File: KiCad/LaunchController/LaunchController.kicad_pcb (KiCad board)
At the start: 2 copper layers, 150 x 100 mm, 164 parts, among them J1 CONN_ICSP, J10 CONN_AUDIO, J11 RJ45, J12 CONN_SPEAKER, J2 CONN_USB, J3 USB_B_Micro, J4 DC_IN, J5 TO_CONVERTER, J6 FROM_CONVERTER, J7 CONN_STATUS_PANEL, J8 CONN_PANEL_BAORD_2, J9 CONN_PANEL_BAORD_1, Q1 TJ8S06M3L, Q2 TJ8S06M3L, Q3 2SC3325-Y, SW1 SW_Push, SW11 SW_Push, SW12 SW_Push, SW13 SW_Push, SW14 SW_Push, SW15 SW_Push, SW16 SW_Push, SW17 SW_Push, SW18 SW_Push, SW19 SW_Push, SW2 SW_Push, SW20 SW_Push, SW21 SW_Push, SW22 SW_Push, SW23 SW_Push, SW24 SW_Push, SW25 SW_Push, U1 FT232RL, U2 ATMEGA2560-16AUR, U3 NJM7805SDL1, U4 INA219BIDCNT, U5 INA219BIDCNT, U6 DFPlayer, U7 24LC256, U8 LTC485CN8#PBF, Y1 HUSG-16.000-20

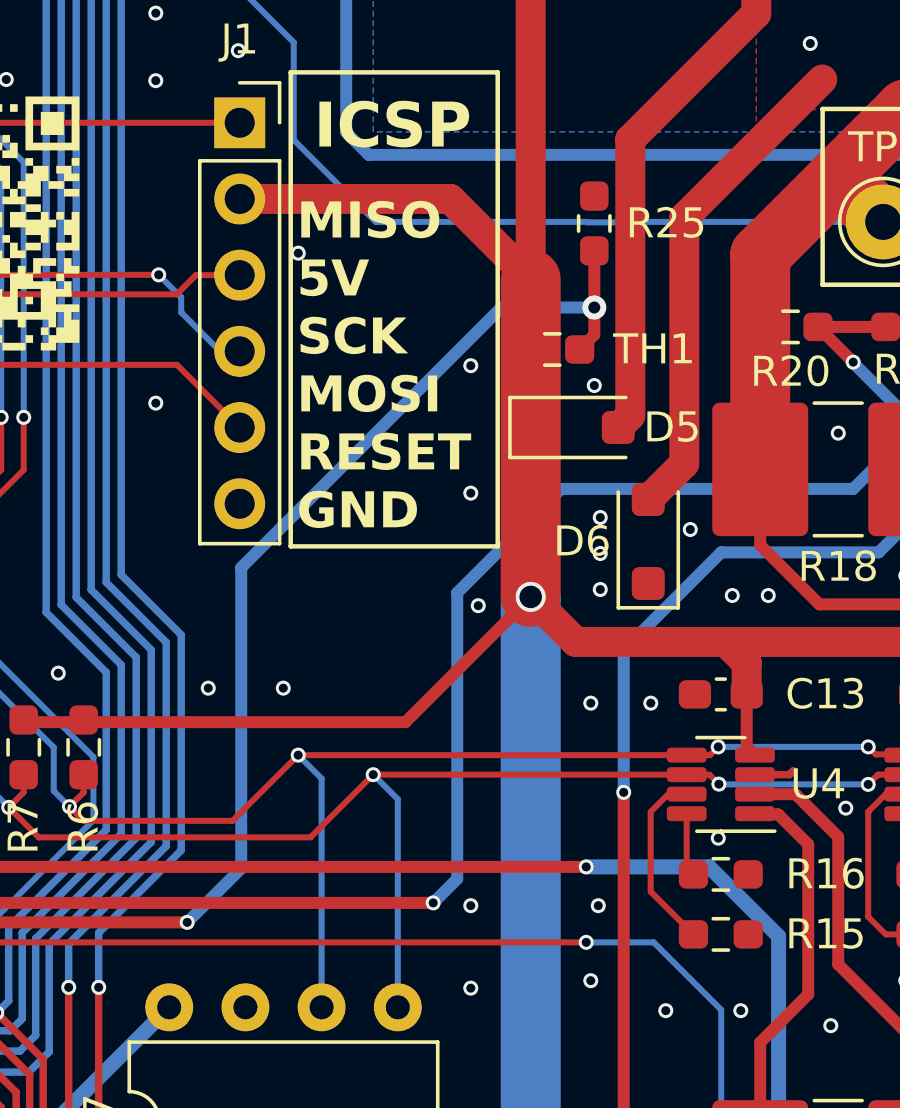
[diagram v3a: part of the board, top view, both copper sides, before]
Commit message: サーミスタを分圧の下流側に変更
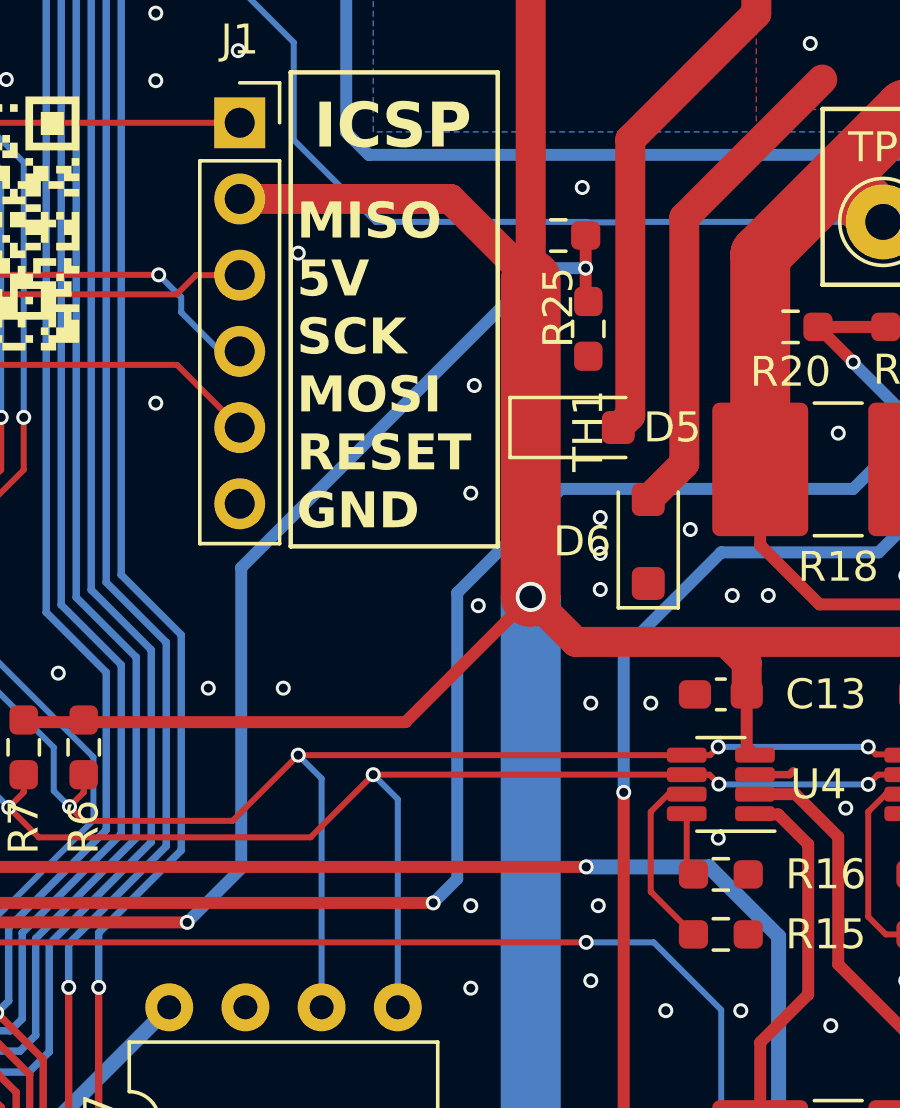
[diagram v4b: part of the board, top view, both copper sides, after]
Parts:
- moved TH1 1.38 mm to (157.8, 66.9), turned to -90 degrees
- moved R25 1.26 mm to (156.8, 63.8), turned to 180 degrees
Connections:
- R25 pad 1: GND -> VREF_THERMISTOR
- R25 pad 2: VREF_THERMISTOR -> CONN_LED_5V
- TH1 pad 1: CONN_LED_5V -> VREF_THERMISTOR
- TH1 pad 2: VREF_THERMISTOR -> GND
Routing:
- net VREF_THERMISTOR: track 46.9 -> 45.9 mm
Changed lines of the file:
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@@
   )
   (footprint "Resistor_SMD:R_0603_1608Metric_Pad0.98x0.95mm_HandSolder" (layer "F.Cu")
-    (at 156.6 67.6)
+    (at 157.8 66.9125 -90)
     (descr "Resistor SMD 0603 (1608 Metric), square (rectangular) end terminal, IPC_7351 nominal with elongated pad for handsoldering. (Body size source: IPC-SM-782 page 72, https://www.pcb-3d.com/wordpress/wp-content/uploads/ipc-sm-782a_amendment_1_and_2.pdf), generated with kicad-footprint-generator")
     (tags "resistor handsolder")
@@
     (property "ki_keywords" "thermistor NTC resistor sensor RTD")
     (attr smd)
-    (fp_text reference "TH1" (at 3.4 0 180) (layer "F.SilkS")
+    (fp_text reference "TH1" (at 3.4 0 90) (layer "F.SilkS")
         (effects (font (size 1 1) (thickness 0.15)))
     )
-    (fp_text value "10kR" (at 0 1.43) (layer "F.Fab")
+    (fp_text value "10kR" (at 0 1.43 90) (layer "F.Fab")
         (effects (font (size 1 1) (thickness 0.15)))
     )
-    (fp_text user "${REFERENCE}" (at 0 0) (layer "F.Fab")
+    (fp_text user "${REFERENCE}" (at 0 0 90) (layer "F.Fab")
         (effects (font (size 0.4 0.4) (thickness 0.06)))
     )
@@
     (fp_line (start 0.8 0.4125) (end -0.8 0.4125)
       (stroke (width 0.1) (type solid)) (layer "F.Fab"))
-    (pad "1" smd roundrect (at -0.9125 0) (size 0.975 0.95) (layers "F.Cu" "F.Paste" "F.Mask") (roundrect_rratio 0.25)
-      (net 40 "CONN_LED_5V") (pintype "passive"))
-    (pad "2" smd roundrect (at 0.9125 0) (size 0.975 0.95) (layers "F.Cu" "F.Paste" "F.Mask") (roundrect_rratio 0.25)
+    (pad "1" smd roundrect (at -0.9125 0 270) (size 0.975 0.95) (layers "F.Cu" "F.Paste" "F.Mask") (roundrect_rratio 0.25)
       (net 71 "VREF_THERMISTOR") (pintype "passive"))
+    (pad "2" smd roundrect (at 0.9125 0 270) (size 0.975 0.95) (layers "F.Cu" "F.Paste" "F.Mask") (roundrect_rratio 0.25)
+      (net 1 "GND") (pintype "passive"))
     (model "${KICAD6_3DMODEL_DIR}/Resistor_SMD.3dshapes/R_0603_1608Metric.wrl"
       (offset (xyz 0 0 0))
@@
   )
   (footprint "Resistor_SMD:R_0603_1608Metric_Pad0.98x0.95mm_HandSolder" (layer "F.Cu")
-    (at 158 63.4 -90)
+    (at 156.8 63.8 180)
     (descr "Resistor SMD 0603 (1608 Metric), square (rectangular) end terminal, IPC_7351 nominal with elongated pad for handsoldering. (Body size source: IPC-SM-782 page 72, https://www.pcb-3d.com/wordpress/wp-content/uploads/ipc-sm-782a_amendment_1_and_2.pdf), generated with kicad-footprint-generator")
     (tags "resistor handsolder")
@@
     (property "ki_keywords" "R resistor")
     (attr smd)
-    (fp_text reference "R25" (at 0 -2.4) (layer "F.SilkS")
+    (fp_text reference "R25" (at 0 -2.4 90) (layer "F.SilkS")
         (effects (font (size 1 1) (thickness 0.15)))
     )
-    (fp_text value "10kR" (at 0 1.43 90) (layer "F.Fab")
+    (fp_text value "10kR" (at 0 1.43) (layer "F.Fab")
         (effects (font (size 1 1) (thickness 0.15)))
     )
-    (fp_text user "${REFERENCE}" (at 0 0 90) (layer "F.Fab")
+    (fp_text user "${REFERENCE}" (at 0 0) (layer "F.Fab")
         (effects (font (size 0.4 0.4) (thickness 0.06)))
     )
@@
     (fp_line (start 0.8 0.4125) (end -0.8 0.4125)
       (stroke (width 0.1) (type solid)) (layer "F.Fab"))
-    (pad "1" smd roundrect (at -0.9125 0 270) (size 0.975 0.95) (layers "F.Cu" "F.Paste" "F.Mask") (roundrect_rratio 0.25)
-      (net 1 "GND") (pintype "passive"))
-    (pad "2" smd roundrect (at 0.9125 0 270) (size 0.975 0.95) (layers "F.Cu" "F.Paste" "F.Mask") (roundrect_rratio 0.25)
+    (pad "1" smd roundrect (at -0.9125 0 180) (size 0.975 0.95) (layers "F.Cu" "F.Paste" "F.Mask") (roundrect_rratio 0.25)
       (net 71 "VREF_THERMISTOR") (pintype "passive"))
+    (pad "2" smd roundrect (at 0.9125 0 180) (size 0.975 0.95) (layers "F.Cu" "F.Paste" "F.Mask") (roundrect_rratio 0.25)
+      (net 40 "CONN_LED_5V") (pintype "passive"))
     (model "${KICAD6_3DMODEL_DIR}/Resistor_SMD.3dshapes/R_0603_1608Metric.wrl"
       (offset (xyz 0 0 0))
@@
   (via (at 77.8 71.2) (size 0.5) (drill 0.3) (layers "F.Cu" "B.Cu") (free) (net 1))
   (via (at 127.883174 91.638716) (size 0.5) (drill 0.3) (layers "F.Cu" "B.Cu") (free) (net 1))
-  (via (at 153.883174 68.138716) (size 0.5) (drill 0.3) (layers "F.Cu" "B.Cu") (free) (net 1))
+  (via (at 154 68.8) (size 0.5) (drill 0.3) (layers "F.Cu" "B.Cu") (free) (net 1))
   (via (at 162.883174 89.638716) (size 0.5) (drill 0.3) (layers "F.Cu" "B.Cu") (free) (net 1))
   (via (at 91.4 86) (size 0.5) (drill 0.3) (layers "F.Cu" "B.Cu") (free) (net 1))
@@
   (via (at 88.6 40) (size 0.5) (drill 0.3) (layers "F.Cu" "B.Cu") (free) (net 1))
   (via (at 156.633174 122.388716) (size 0.5) (drill 0.3) (layers "F.Cu" "B.Cu") (free) (net 1))
-  (via (at 158 68.8) (size 0.5) (drill 0.3) (layers "F.Cu" "B.Cu") (free) (net 1))
   (via (at 172.4 112.8) (size 0.5) (drill 0.3) (layers "F.Cu" "B.Cu") (free) (net 1))
   (via (at 107 110) (size 0.5) (drill 0.3) (layers "F.Cu" "B.Cu") (free) (net 1))
   (via (at 191.383174 99.138716) (size 0.5) (drill 0.3) (layers "F.Cu" "B.Cu") (free) (net 1))
   (via (at 181.633174 99.388716) (size 0.5) (drill 0.3) (layers "F.Cu" "B.Cu") (free) (net 1))
+  (via (at 157.6 62.2) (size 0.5) (drill 0.3) (layers "F.Cu" "B.Cu") (free) (net 1))
   (via (at 84.8 83.8) (size 0.5) (drill 0.3) (layers "F.Cu" "B.Cu") (free) (net 1))
   (via (at 70.8 88.4) (size 0.5) (drill 0.3) (layers "F.Cu" "B.Cu") (free) (net 1))
@@
   (segment (start 131.955974 86.636526) (end 129.81668 84.497232) (width 0.25) (layer "F.Cu") (net 71))
   (segment (start 132.015741 86.696293) (end 144.430707 86.696293) (width 0.4) (layer "F.Cu") (net 71))
+  (segment (start 157.7125 64.8875) (end 157.7125 65.9125) (width 0.4) (layer "F.Cu") (net 71))
+  (segment (start 157.7125 65.9125) (end 157.8 66) (width 0.4) (layer "F.Cu") (net 71))
+  (segment (start 157.7125 64.8875) (end 157.7125 63.8) (width 0.4) (layer "F.Cu") (net 71))
   (segment (start 131.955974 86.636526) (end 132.015741 86.696293) (width 0.4) (layer "F.Cu") (net 71))
-  (segment (start 158 67.1125) (end 158 64.3125) (width 0.4) (layer "F.Cu") (net 71))
-  (segment (start 157.5125 67.6) (end 158 67.1125) (width 0.4) (layer "F.Cu") (net 71))
-  (via (at 158 66.2) (size 0.8) (drill 0.4) (layers "F.Cu" "B.Cu") (net 71))
+  (via (at 157.7125 64.8875) (size 0.5) (drill 0.3) (layers "F.Cu" "B.Cu") (net 71))
   (via (at 144.430707 86.696293) (size 0.5) (drill 0.3) (layers "F.Cu" "B.Cu") (net 71))
-  (segment (start 144.430707 86.696293) (end 146.230707 84.896293) (width 0.4) (layer "B.Cu") (net 71))
   (segment (start 146.230707 74.871944) (end 146.230707 84.896293) (width 0.4) (layer "B.Cu") (net 71))
-  (segment (start 154.902651 66.2) (end 146.230707 74.871944) (width 0.4) (layer "B.Cu") (net 71))
-  (segment (start 158 66.2) (end 154.902651 66.2) (width 0.4) (layer "B.Cu") (net 71))
+  (segment (start 146.230707 84.896293) (end 144.430707 86.696293) (width 0.4) (layer "B.Cu") (net 71))
+  (segment (start 156.215151 64.8875) (end 146.230707 74.871944) (width 0.4) (layer "B.Cu") (net 71))
+  (segment (start 157.7125 64.8875) (end 156.215151 64.8875) (width 0.4) (layer "B.Cu") (net 71))
   (segment (start 76.735 64.875) (end 76.735 62.8375) (width 0.2) (layer "F.Cu") (net 72))
   (segment (start 65.735 64.875) (end 65.735 62.8375) (width 0.2) (layer "F.Cu") (net 73))

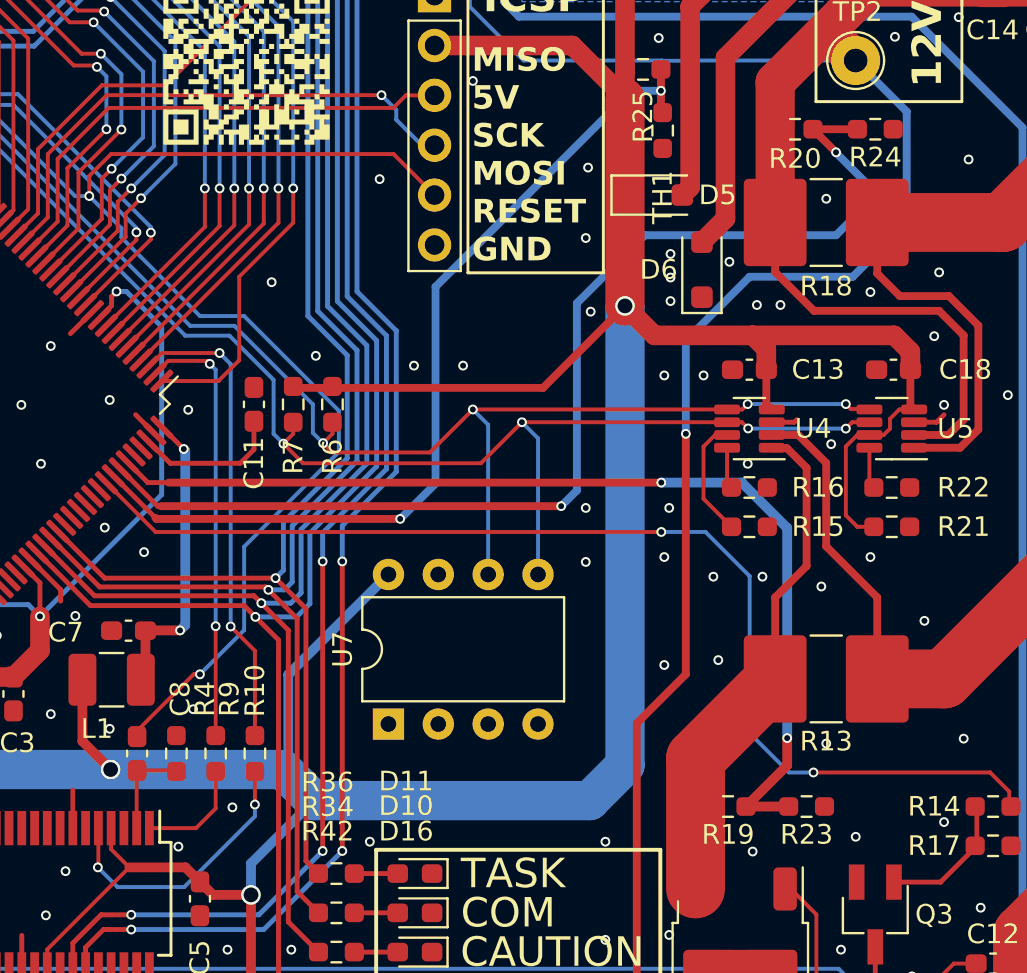
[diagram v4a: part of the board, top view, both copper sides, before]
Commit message: イラン分圧回路を削除
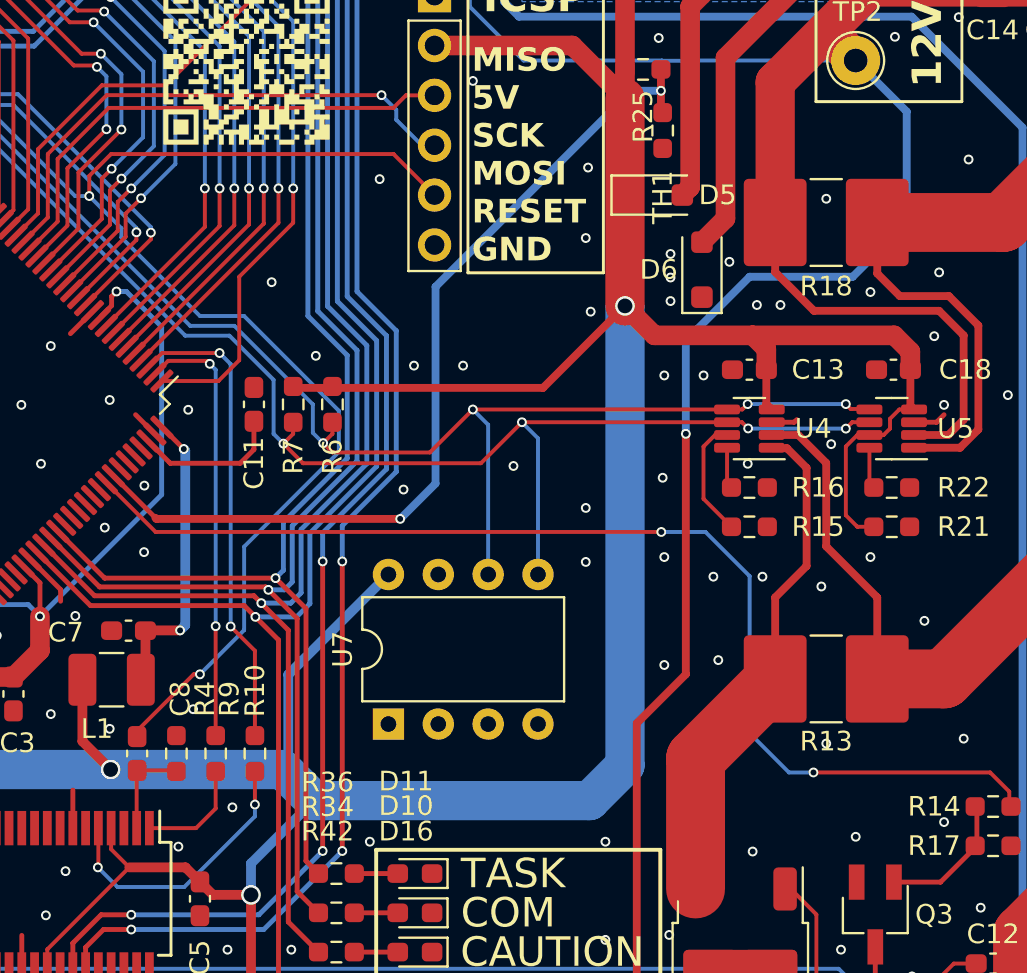
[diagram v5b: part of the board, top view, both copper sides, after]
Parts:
- removed R19, R20: 12kR, Resistor_SMD:R_0603_1608Metric_Pad0.98x0.95mm_HandSolder
- removed R23, R24: 2kR, Resistor_SMD:R_0603_1608Metric_Pad0.98x0.95mm_HandSolder
- R34, R36: value 1kR -> 2.2kR
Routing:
- net VREF_12V: track 58.0 -> 0.00 mm, vias 2 -> 0
- net VREF_VSW: track 52.2 -> 0.00 mm, vias 2 -> 0
- net GND: vias 283 -> 286

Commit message: RJ45をヒロセに変更
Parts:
- J11: footprint Connector_RJ:RJ45_Wuerth_7499010001A_Horizontal -> TSRP_Connector_Hirose:TM11R-5M2-88
- moved J11 9.21 mm to (97.8, 119.0), turned to 0 degrees
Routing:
- net Net-(U8-A): track 14.1 -> 23.4 mm
- net Net-(U8-B): track 24.1 -> 26.5 mm
